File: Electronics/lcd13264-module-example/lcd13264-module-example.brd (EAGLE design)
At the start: 99.1 x 99.1 mm, 5 parts

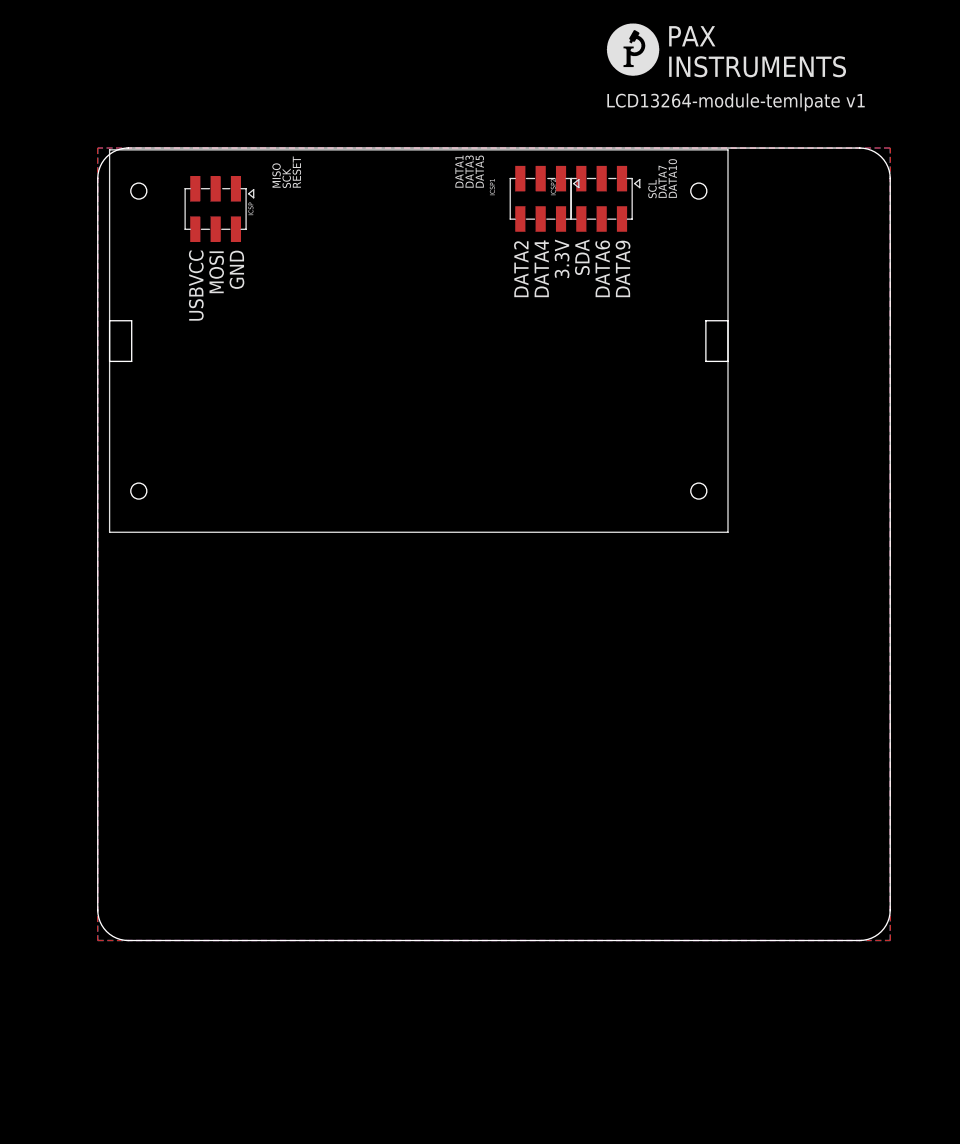
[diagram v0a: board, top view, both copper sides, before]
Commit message: Added an example board using the LCD module template. Just headers, a buzzer, breadboards, and buttons.
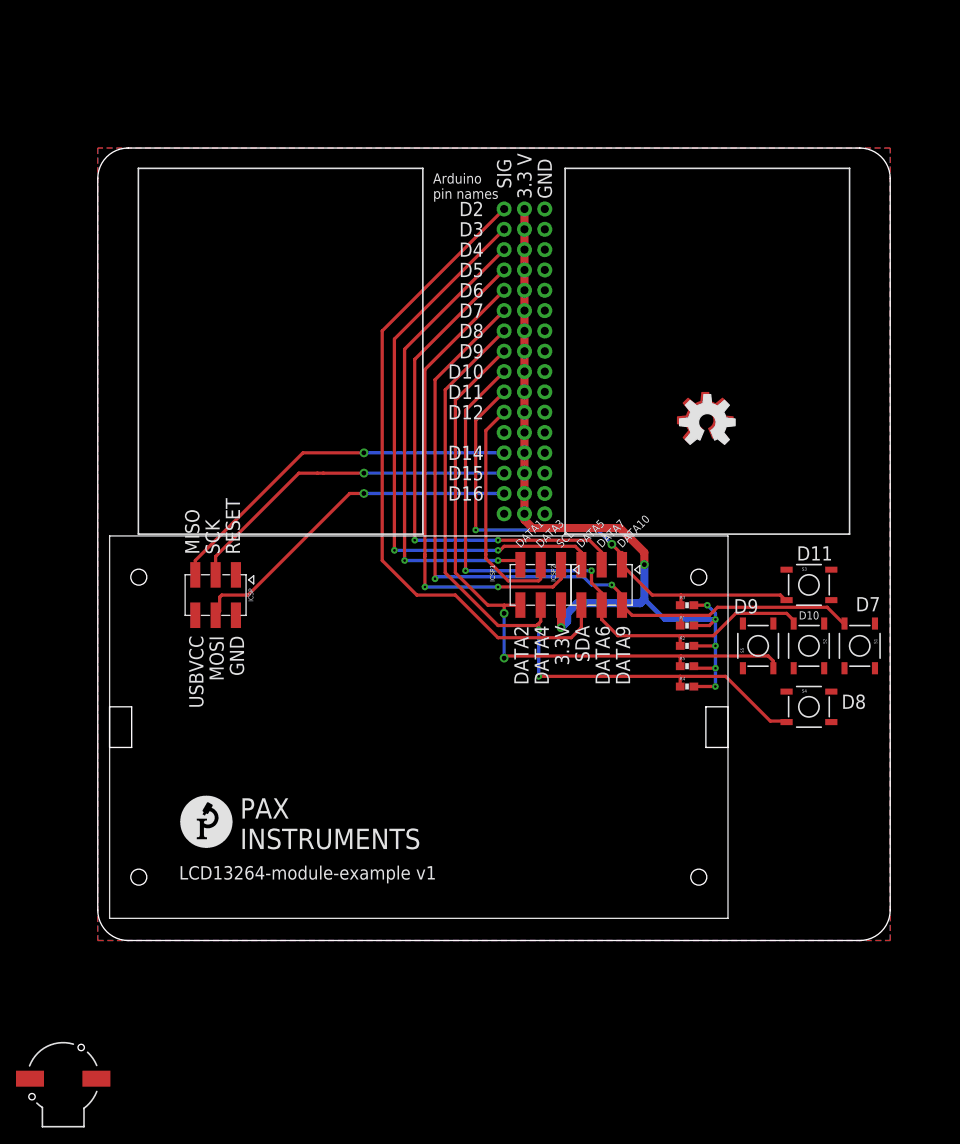
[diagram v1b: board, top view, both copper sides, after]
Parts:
- added JP1, JP2, JP3: (no value), SparkFun-Connectors:1X16_NO_SILK
- added LOGO1: OSHW-LOGOL, SparkFun-Aesthetics:OSHW-LOGO-L
- added LOGO2: OSHW-LOGOL-COPPER, SparkFun-Aesthetics:OSHW-LOGO-L_COPPER
- added R1, R2, R3, R4, R5: 10k, SparkFun-Passives:0603-RES
- added S1, S2, S3, S4, S5: SWITCH-MOMENTARY-2SMD, SparkFun-Electromechanical:TACTILE-SWITCH-SMD
- added SG1: BUZZERSMD2-KIT, SparkFun-Electromechanical:BUZZER-CCV-KIT
- added U$1, U$2: BREADBOARDMINI, SparkFun-Boards:BREADBOARD-MINI
- moved U$6 110.3 mm to (10.2, 11.4)
- moved U$5 48.3 mm to (40.1, 26.7)
- moved ICSP 48.3 mm to (14.7, 43.2)
- moved ICSP1 48.3 mm to (55.4, 44.5)
- moved ICSP2 48.3 mm to (63.0, 44.5)
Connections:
- new net N$1: SG1.+
- new net N$2: SG1.-
- net 3.3V: now also JP2.1, JP2.10, JP2.11, JP2.12, JP2.13, JP2.14, JP2.15, JP2.16, JP2.2, JP2.3, JP2.4, JP2.5, JP2.6, JP2.7, JP2.8, JP2.9, R1.2, R2.2, R3.2, R4.2, R5.2
- net DATA1: now also JP1.14
- net DATA10: now also JP1.7, R3.1, S3.3
- net DATA2: now also JP1.9, R5.1, S5.3
- net DATA3: now also JP1.6
- net DATA4: now also JP1.10, R4.1, S4.3
- net DATA5: now also JP1.12
- net DATA6: now also JP1.8, R2.1, S2.3
- net DATA7: now also JP1.13
- net DATA9: now also JP1.11, R1.1, S1.3
- net GND: now also JP3.1, JP3.10, JP3.11, JP3.12, JP3.13, JP3.14, JP3.15, JP3.16, JP3.2, JP3.3, JP3.4, JP3.5, JP3.6, JP3.7, JP3.8, JP3.9, S1.1, S2.1, S3.1, S4.1, S5.1
- net MISO: now also JP1.4
- net MOSI: now also JP1.2
- net SCK: now also JP1.3
- net SCL: now also JP1.15
- net SDA: now also JP1.16
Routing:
- net 3.3V: track 0.00 -> 110.1 mm, vias 0 -> 7
- net DATA9: track 0.00 -> 94.1 mm, vias 0 -> 2
- net DATA4: track 0.00 -> 91.4 mm, vias 0 -> 2
- net DATA2: track 0.00 -> 82.9 mm, vias 0 -> 2
- net SDA: track 0.00 -> 82.5 mm
- net DATA6: track 0.00 -> 77.3 mm, vias 0 -> 2
- net SCL: track 0.00 -> 71.3 mm, vias 0 -> 2
- net DATA7: track 0.00 -> 64.0 mm, vias 0 -> 2
- net DATA10: track 0.00 -> 63.6 mm, vias 0 -> 2
- net DATA5: track 0.00 -> 60.4 mm, vias 0 -> 2
- net DATA1: track 0.00 -> 58.7 mm, vias 0 -> 2
- net MISO: track 0.00 -> 46.0 mm, vias 0 -> 1
- net MOSI: track 0.00 -> 43.4 mm, vias 0 -> 1
- net SCK: track 0.00 -> 42.7 mm, vias 0 -> 1
- net DATA3: track 0.00 -> 29.1 mm
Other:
- board text added: "3.3 V"
- board text added: "Arduino pin names"
- board text added: "D10"
- board text added: "D11"
- board text added: "D12"
- board text added: "D14"
- board text added: "D15"
- board text added: "D16"
- board text added: "D2"
- board text added: "D3"
- board text added: "D4"
- board text added: "D5"
- board text added: "D6"
- board text added: "D7"
- board text added: "D8"
- board text added: "D9"
- board text added: "LCD13264-module-example v1"
- board text added: "SIG"
- board text removed: "LCD13264-module-temlpate v1"
